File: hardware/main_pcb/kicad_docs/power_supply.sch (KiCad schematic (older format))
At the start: 1 part, among them J13 9vdc_in

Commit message: progress on schemo
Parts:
- added U8: TLV1117-33, Package_TO_SOT_SMD:SOT-223-3_TabPin2, symbol Regulator_Linear:TLV1117-33
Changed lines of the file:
@@
 	-1   0    0    -1
 $EndComp
+$Comp
+L Regulator_Linear:TLV1117-33 U8
+U 1 1 5FBA754B
+P 4450 1550
+F 0 "U8" H 4450 1792 50  0000 C CNN
+F 1 "TLV1117-33" H 4450 1701 50  0000 C CNN
+F 2 "Package_TO_SOT_SMD:SOT-223-3_TabPin2" H 4450 1550 50  0001 C CNN
+F 3 "http://www.ti.com/lit/ds/symlink/tlv1117.pdf" H 4450 1550 50  0001 C CNN
+	1    4450 1550
+	1    0    0    -1
+$EndComp
 $EndSCHEMATC

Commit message: progress on pcb layout
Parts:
- removed J13: 9vdc_in, Connector_PinHeader_2.54mm:PinHeader_1x02_P2.54mm_Vertical, symbol Connector_Generic:Conn_01x02
- removed U8: TLV1117-33, Package_TO_SOT_SMD:SOT-223-3_TabPin2, symbol Regulator_Linear:TLV1117-33
- added C10, C12, C15, C17, C18, C20, C23, C4, C46, C47, C48, C49, C5, C50, C51, C52, C53, C54, C55, C6, C7, C8: 100n, Capacitor_SMD:C_0603_1608Metric, symbol Device:C
- added C11, C13, C3, C9: 10u, Capacitor_SMD:C_0805_2012Metric, symbol Device:C
- added C14, C19, C21: 1u, Capacitor_SMD:C_0805_2012Metric, symbol Device:C
- added C16, C22, C24: 4u7, Capacitor_SMD:C_0805_2012Metric, symbol Device:C
- added D1: B5819W, Diode_SMD:D_SOD-123, symbol Device:D_Schottky
- added D2, D3, D4, D5: PMEG2010AEH, Diode_SMD:D_SOD-123F, symbol Diode:PMEG2010AEH
- added FB1, FB2, FB3, FB4: 100R @ 100MHz, Inductor_SMD:L_0805_2012Metric, symbol Device:Ferrite_Bead_Small
- added L1: 10uH, 1.2A, Inductor_SMD:L_Taiyo-Yuden_NR-50xx, symbol pspice:INDUCTOR
- added R10: 13k3, Resistor_SMD:R_0603_1608Metric, symbol Device:R
- added R11: 20k, Resistor_SMD:R_0603_1608Metric, symbol Device:R
- added R5: 2k2, Resistor_SMD:R_0603_1608Metric, symbol Device:R
- added R6, R7: 1R, Resistor_SMD:R_0603_1608Metric, symbol Device:R
- added R8: 100k, Resistor_SMD:R_0603_1608Metric, symbol Device:R
- added R9: 114k, Resistor_SMD:R_0603_1608Metric, symbol Device:R
- added U1: TL074, Package_SO:TSSOP-14_4.4x5mm_P0.65mm, symbol Amplifier_Operational:TL074
- added U12: LT1117-3.3, Package_TO_SOT_SMD:SOT-223-3_TabPin2, symbol Regulator_Linear:LT1117-3.3
- added U13: LT3467A, Package_TO_SOT_SMD:TSOT-23-6, symbol custom_components:LT3467A
- added U14: LM4040DBZ-5, Package_TO_SOT_SMD:SOT-23, symbol Reference_Voltage:LM4040DBZ-5
- added U2, U3, U4, U5: MCP6004, Package_SO:TSSOP-14_4.4x5mm_P0.65mm, symbol Amplifier_Operational:MCP6004
- added U6, U7, U8, U9: DG469EQ, Package_SO:MSOP-8_3x3mm_P0.65mm, symbol custom_components:DG469EQ
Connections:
- new net: C11.1, FB1.1, U12.3 (VI)
- new net: C18.2, FB4.2, R5.2
- new net: C16.1, FB3.1, L1.1, U13.4 (~SHDN), U13.6 (Vin)
- new net: C17.1, U13.5 (SS)
- new net: C19.1, C21.2, L1.2, U13.1 (SW)
- new net: C19.2, D2.2 (A), R6.1
- new net: C21.1, D4.2 (A), R7.2
- new net: D3.1 (K), R7.1
- new net: R10.2, R9.1, U13.3 (FB)
- new net: D5.1 (K), R6.2
- new net: C23.2, R11.2, R8.1, U5.6 (-)
- new net +12V: C24.1, C4.1, C48.1, C50.1, C52.1, C54.1, D4.1 (K), R9.2, U1.4 (V+), U6.4 (V+), U7.4 (V+), U8.4 (V+), U9.4 (V+)
- new net +1V0: C23.1, R11.1, U5.7
- new net +3.3VA: C14.1, C15.1, FB2.1
- new net +3V3: C10.1, C12.1, C13.1, C3.1, C46.1, C47.1, C6.1, C7.1, C8.1, C9.1, FB2.2, U12.2 (VO), U2.4 (V+), U3.4 (V+), U4.4 (V+), U5.4 (V+)
- new net +9V: D1.1 (K), FB1.2, FB3.2
- new net -12V: C22.2, C49.2, C5.2, C51.2, C53.2, C55.2, D5.2 (A), FB4.1, U1.11 (V-), U6.7 (V-), U7.7 (V-), U8.7 (V-), U9.7 (V-)
- new net -5V: C20.2, R5.1, R8.2, U14.2 (A)
- new net 9VDC_in: D1.2 (A)
- new net GND: C10.2, C11.2, C12.2, C13.2, C14.2, C15.2, C16.2, C17.2, C18.1, C20.1, C22.1, C24.2, C3.2, C4.2, C46.2, C47.2, C48.2, C49.1, C5.1, C50.2, C51.1, C52.2, C53.1, C54.2, C55.1, C6.2, C7.2, C8.2, C9.2, D2.1 (K), D3.2 (A), R10.1, U12.1 (GND), U13.2 (GND), U14.1 (K), U2.11 (V-), U3.11 (V-), U4.11 (V-), U5.11 (V-), U5.5 (+), U6.3 (GND), U7.3 (GND), U8.3 (GND), U9.3 (GND)
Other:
- note added: "+/-12 volt DC-DC converter"
- note added: "+1 volt reference"
- note added: "+3.3 volt regulator"
- note added: "+9 volt power entry"
- note added: "-5 volt reference"
- note added: "DAC decoupling"
- note added: "STM32 decoupling"
- note added: "analog switches"
- note added: "opamps"

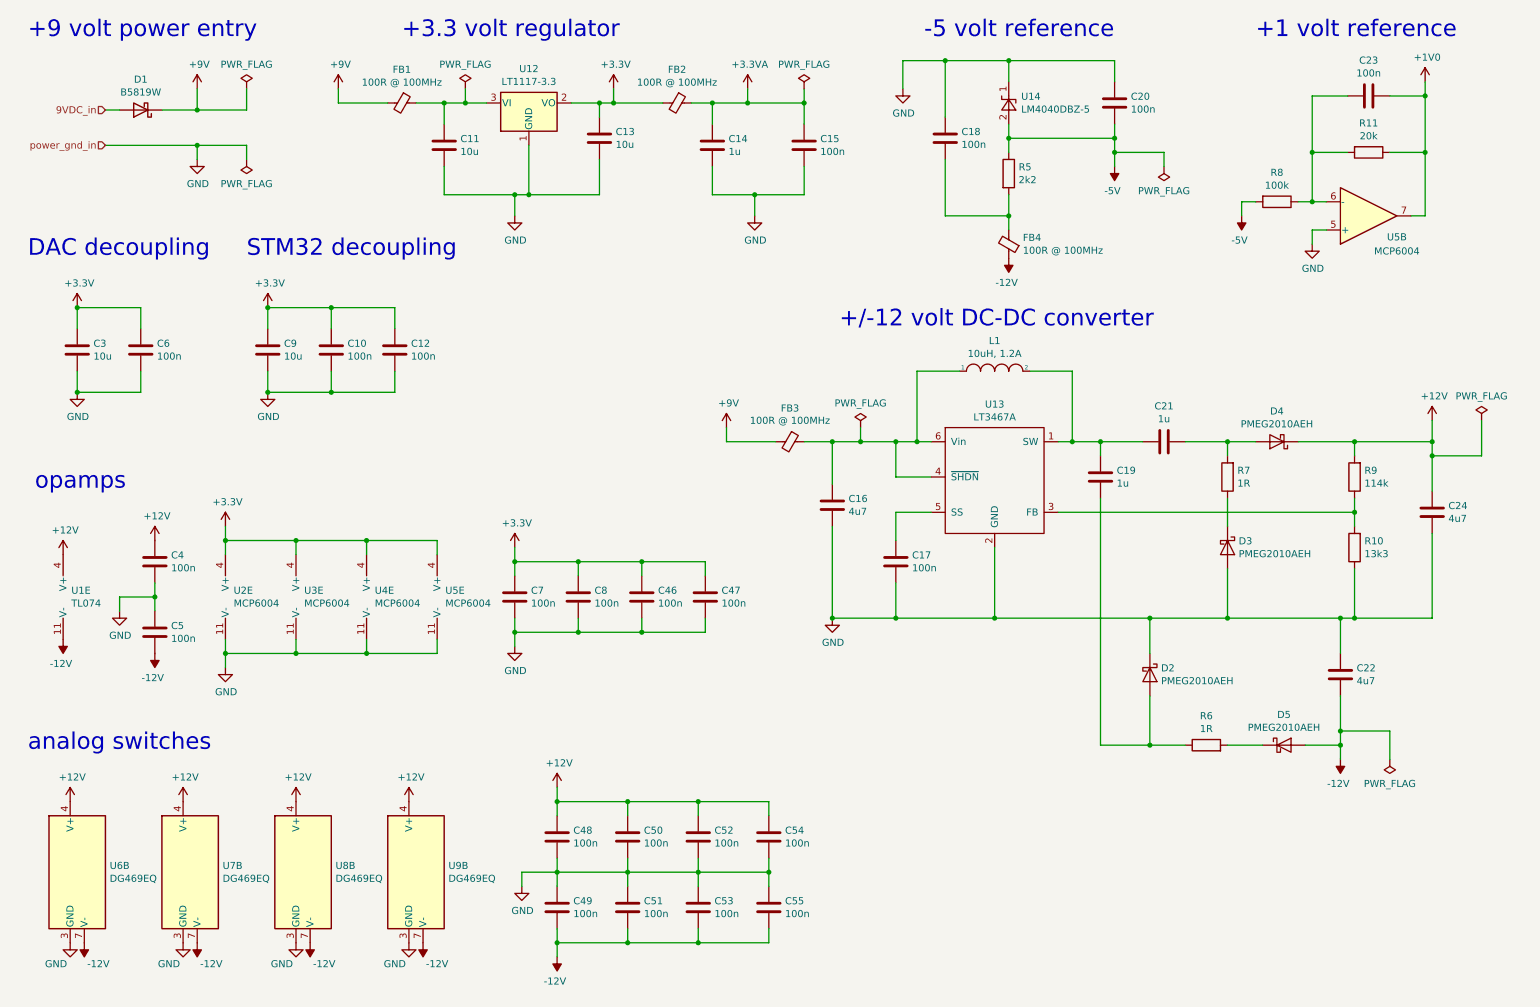
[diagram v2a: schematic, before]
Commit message: reduce analog switch count, tidy up
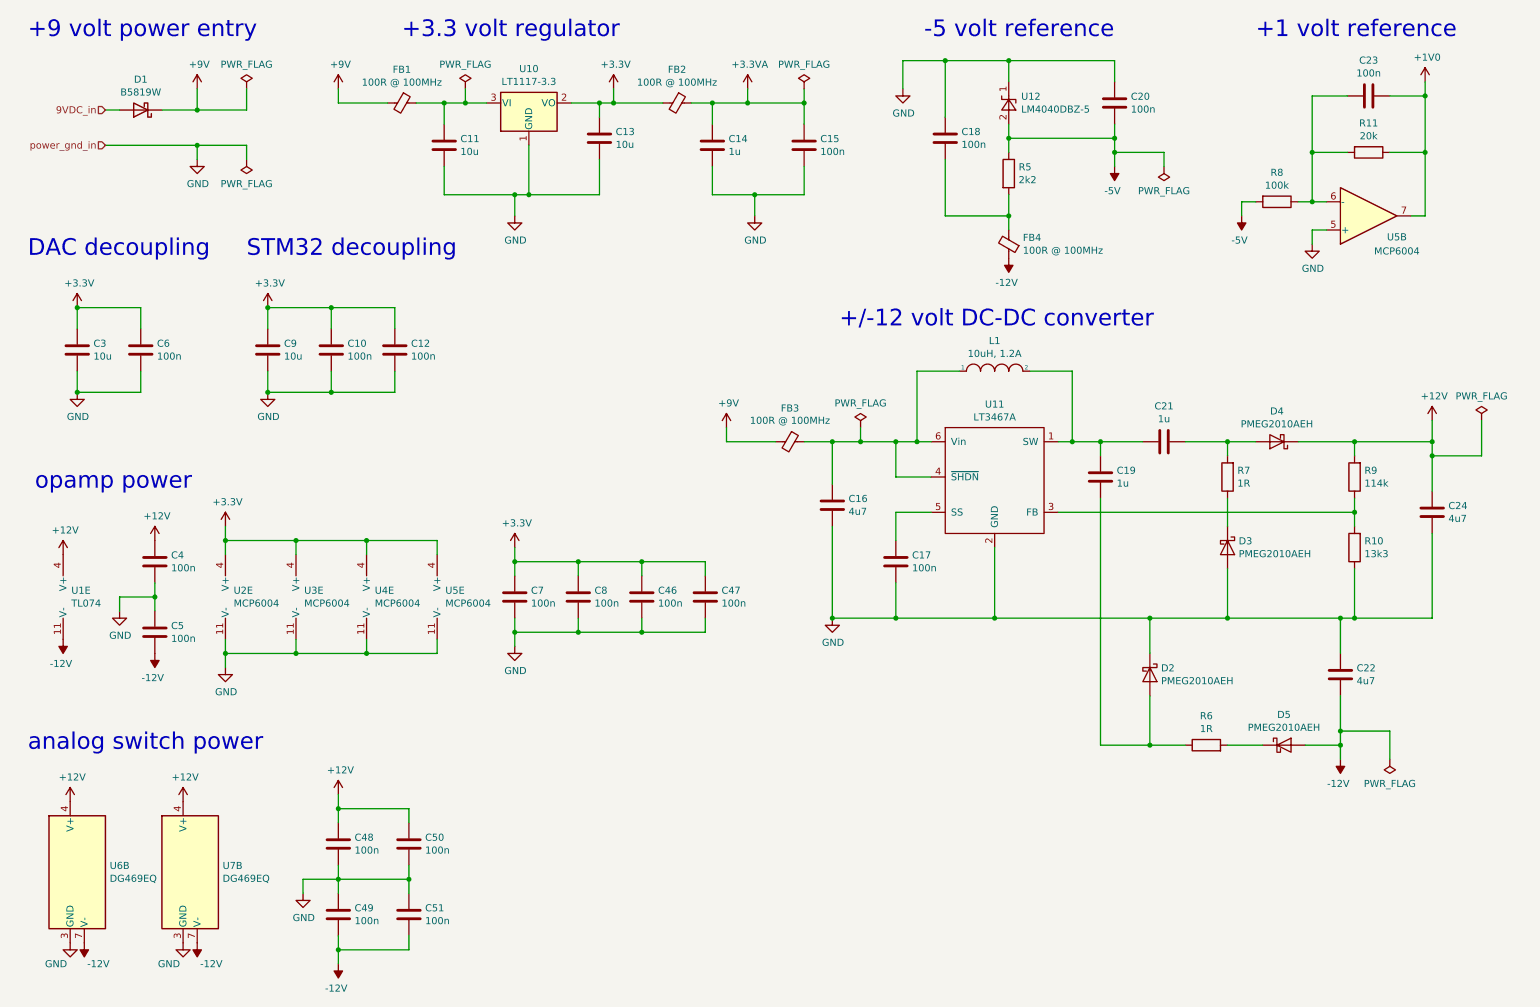
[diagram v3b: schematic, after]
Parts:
- removed C52, C53, C54, C55: 100n, Capacitor_SMD:C_0603_1608Metric, symbol Device:C
- removed U8, U9: DG469EQ, Package_SO:MSOP-8_3x3mm_P0.65mm, symbol custom_components:DG469EQ
- renumbered U12 to U10, U13 to U11, U14 to U12
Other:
- note added: "analog switch power"
- note added: "opamp power"
- note removed: "analog switches"
- note removed: "opamps"
- moved on the sheet: C48, C49, C50, C51

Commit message: tidy up kicad docs
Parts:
- renumbered C48 to C27, C49 to C29, C50 to C30, C51 to C32
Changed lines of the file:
@@
 $EndComp
 $Comp
-L Device:C C48
+L Device:C C27
 U 1 1 617C76C7
 P 2850 6500
-F 0 "C48" H 2965 6546 50  0000 L CNN
+F 0 "C27" H 2965 6546 50  0000 L CNN
 F 1 "100n" H 2965 6455 50  0000 L CNN
 F 2 "Capacitor_SMD:C_0603_1608Metric" H 2888 6350 50  0001 C CNN
@@
 $EndComp
 $Comp
-L Device:C C49
+L Device:C C29
 U 1 1 617C76CD
 P 2850 7000
-F 0 "C49" H 2965 7046 50  0000 L CNN
+F 0 "C29" H 2965 7046 50  0000 L CNN
 F 1 "100n" H 2965 6955 50  0000 L CNN
 F 2 "Capacitor_SMD:C_0603_1608Metric" H 2888 6850 50  0001 C CNN
@@
 	2600 6750 2850 6750
 $Comp
-L Device:C C50
+L Device:C C30
 U 1 1 617D4458
 P 3350 6500
-F 0 "C50" H 3465 6546 50  0000 L CNN
+F 0 "C30" H 3465 6546 50  0000 L CNN
 F 1 "100n" H 3465 6455 50  0000 L CNN
 F 2 "Capacitor_SMD:C_0603_1608Metric" H 3388 6350 50  0001 C CNN
@@
 $EndComp
 $Comp
-L Device:C C51
+L Device:C C32
 U 1 1 617D4A8E
 P 3350 7000
-F 0 "C51" H 3465 7046 50  0000 L CNN
+F 0 "C32" H 3465 7046 50  0000 L CNN
 F 1 "100n" H 3465 6955 50  0000 L CNN
 F 2 "Capacitor_SMD:C_0603_1608Metric" H 3388 6850 50  0001 C CNN
